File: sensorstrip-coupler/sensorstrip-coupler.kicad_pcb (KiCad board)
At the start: 2 copper layers, 10 x 20 mm, 2 parts, among them J1 Conn_01x02_MountingPin, J2 Conn_01x02_MountingPin

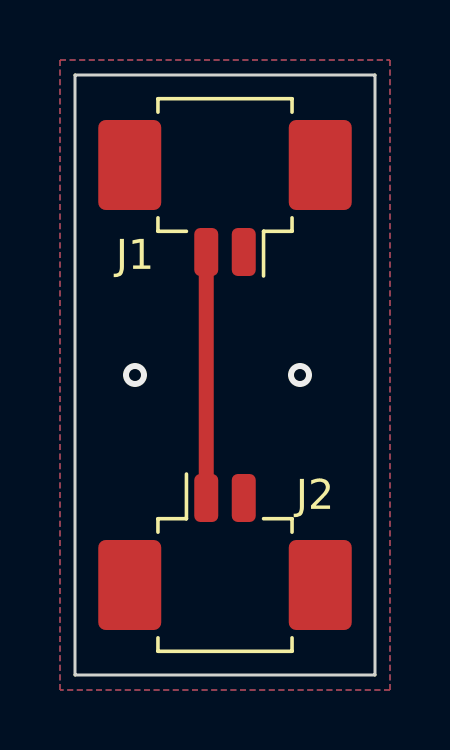
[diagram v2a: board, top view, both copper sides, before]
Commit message: Rename sender / receiver boards to power-emitter and emitter
...hopefully this is clearer

Also some tidying of older boards
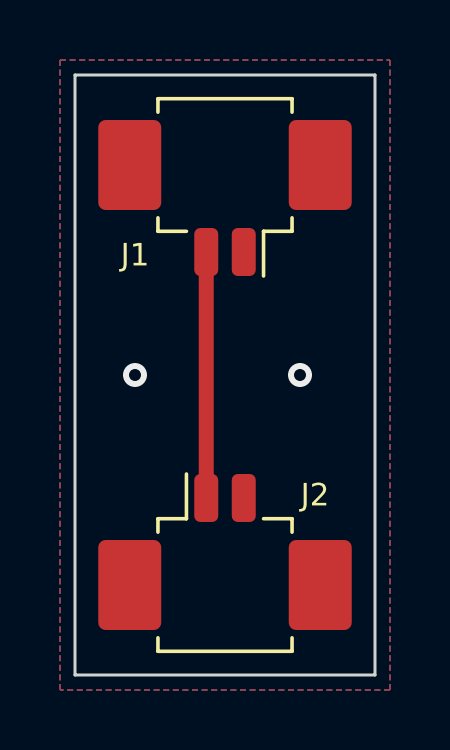
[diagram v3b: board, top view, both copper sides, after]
